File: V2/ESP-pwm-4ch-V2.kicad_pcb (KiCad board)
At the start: 2 copper layers, 103 x 67.8 mm, 39 parts, among them J1 12VDC, J2 OUT1, J3 OUT2, J4 OUT3, J5 OUT4, Q1 IRLB8721PBF, Q2 IRLB8721PBF, Q3 IRLB8721PBF, Q4 IRLB8721PBF, U1 L78M05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

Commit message: pcb tweaks
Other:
- board text added: "ESP-PWM-4CH-V2"
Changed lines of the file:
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@@
     (effects (font (size 1.5 1.1) (thickness 0.25)))
+  )
+  (gr_text "ESP-PWM-4CH-V2" (at 82.55 116.84) (layer "F.SilkS")
+    (effects (font (size 1.2 1.2) (thickness 0.2)))
   )
   (gr_text "+ CH3 -" (at 144.78 129.54) (layer "F.SilkS")

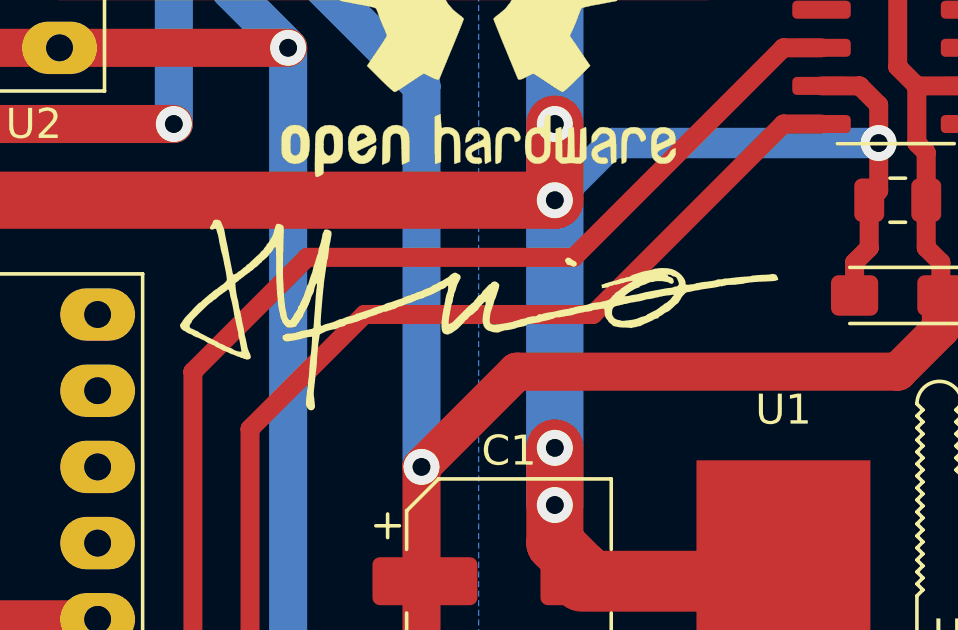
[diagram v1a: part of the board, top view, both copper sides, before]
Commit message: Update ESP-pwm-4ch-V2.kicad_pcb
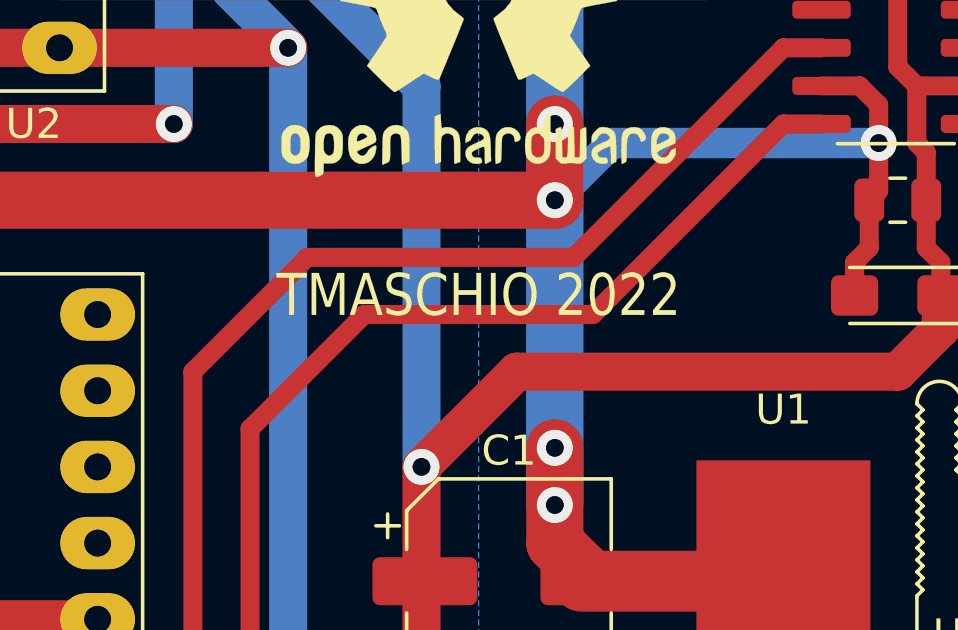
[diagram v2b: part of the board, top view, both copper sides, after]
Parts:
- removed ?: , Tales:TMaschio_20x6.4mm
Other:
- board text added: "TMASCHIO 2022"
